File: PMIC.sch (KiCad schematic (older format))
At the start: 71 parts, among them U4 CSD86330Q3D, U5 LMR62014XMF_NOPB, U6 CSD86330Q3D, U8 TPS65086100

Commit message: Updated GPIO pinout to BV0.9. Remapped DSI. Mapped USB3.0
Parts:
- R121: footprint antmicro-footprints:0402-res -> arvsom-footprints:0402-res; symbol antmicroResistors0402:R_1k_0402 -> arvsom:R_1k_0402
- R123: footprint antmicro-footprints:0402-res -> arvsom-footprints:0402-res; symbol antmicroResistors0402:R_0R_0402 -> arvsom:R_0R_0402
- R13: footprint antmicro-footprints:0402-res -> arvsom-footprints:0402-res; symbol antmicroResistors0402:R_12k1_0402 -> arvsom:R_12k1_0402
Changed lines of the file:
@@
 	11025 6075 11375 6075
 $Comp
-L antmicroResistors0402:R_1k_0402 R121
+L arvsom:R_1k_0402 R121
 U 1 1 60BEDFDF
 P 3650 3750
 F 0 "R121" V 3700 4050 60  0000 R CNN
 F 1 "R_1k_0402" H 3650 3600 60  0001 C CNN
-F 2 "antmicro-footprints:0402-res" H 3850 3950 60  0001 L CNN
+F 2 "arvsom-footprints:0402-res" H 3850 3950 60  0001 L CNN
 F 3 "" H 3650 3750 50  0001 C CNN
 F 4 "BOURNS" H 3850 4150 60  0001 L CNN "Manufacturer"
@@
 Connection ~ 3925 4600
 $Comp
-L antmicroResistors0402:R_0R_0402 R123
+L arvsom:R_0R_0402 R123
 U 1 1 60C2519F
 P 5425 5575
 F 0 "R123" H 5375 5700 60  0000 C CNN
 F 1 "R_0R_0402" H 5425 5425 60  0001 C CNN
-F 2 "antmicro-footprints:0402-res" H 5625 5775 60  0001 L CNN
+F 2 "arvsom-footprints:0402-res" H 5625 5775 60  0001 L CNN
 F 3 "" H 5425 5575 50  0001 C CNN
 F 4 "PANASONIC" H 5625 5975 60  0001 L CNN "Manufacturer"
@@
 	5575 5575 5900 5575
 $Comp
-L antmicroResistors0402:R_12k1_0402 R13
+L arvsom:R_12k1_0402 R13
 U 1 1 60C62589
 P 8500 4475
 F 0 "R13" H 8275 4525 60  0000 C CNN
 F 1 "R_12k1_0402" H 8500 4325 60  0001 C CNN
-F 2 "antmicro-footprints:0402-res" H 8700 4675 60  0001 L CNN
+F 2 "arvsom-footprints:0402-res" H 8700 4675 60  0001 L CNN
 F 3 "" H 8500 4475 50  0001 C CNN
 F 4 "MULTICOMP" H 8700 4875 60  0001 L CNN "Manufacturer"

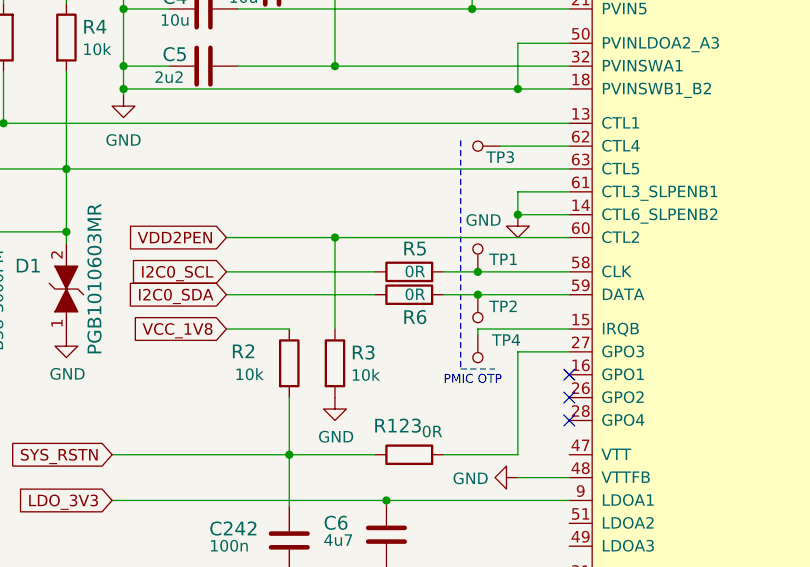
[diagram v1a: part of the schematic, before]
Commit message: Updated ethernet and interfaces.sch
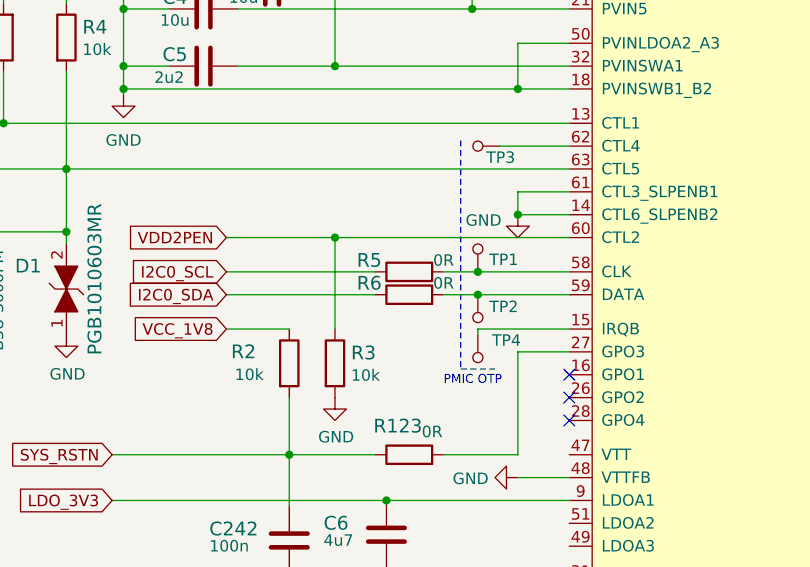
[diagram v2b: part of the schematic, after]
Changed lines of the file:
@@
 U 1 1 6073C6AC
 P 5425 4775
-F 0 "R5" H 5450 4875 60  0000 C CNN
+F 0 "R5" H 5250 4825 60  0000 C CNN
 F 1 "R_0R_0402" H 5425 4625 60  0001 C CNN
 F 2 "arvsom-footprints:0402-res" H 5625 4975 60  0001 L CNN
@@
 F 4 "PANASONIC" H 5625 5175 60  0001 L CNN "Manufacturer"
 F 5 "ERJ2GE0R00X" H 5625 5075 60  0001 L CNN "MPN"
-F 6 "0R" H 5450 4775 50  0000 C CNN "Val"
+F 6 "0R" H 5575 4825 50  0000 C CNN "Val"
 	1    5425 4775
 	1    0    0    -1
@@
 U 1 1 60743B7D
 P 5425 4875
-F 0 "R6" H 5450 4775 60  0000 C CNN
+F 0 "R6" H 5250 4925 60  0000 C CNN
 F 1 "R_0R_0402" H 5425 4725 60  0001 C CNN
 F 2 "arvsom-footprints:0402-res" H 5625 5075 60  0001 L CNN
@@
 F 4 "PANASONIC" H 5625 5275 60  0001 L CNN "Manufacturer"
 F 5 "ERJ2GE0R00X" H 5625 5175 60  0001 L CNN "MPN"
-F 6 "0R" H 5450 4875 50  0000 C CNN "Val"
+F 6 "0R" H 5575 4925 50  0000 C CNN "Val"
 	1    5425 4875
 	1    0    0    -1

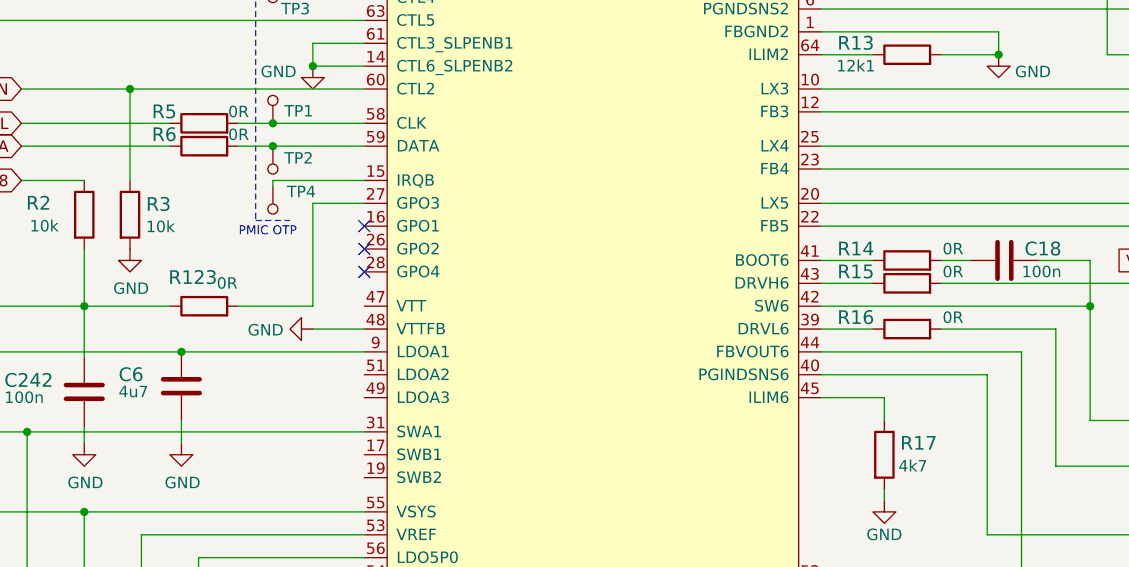
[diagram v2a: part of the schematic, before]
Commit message: Updated component placement - PHY passives placed, moved HDMI IC, lowered VIC and DDRs
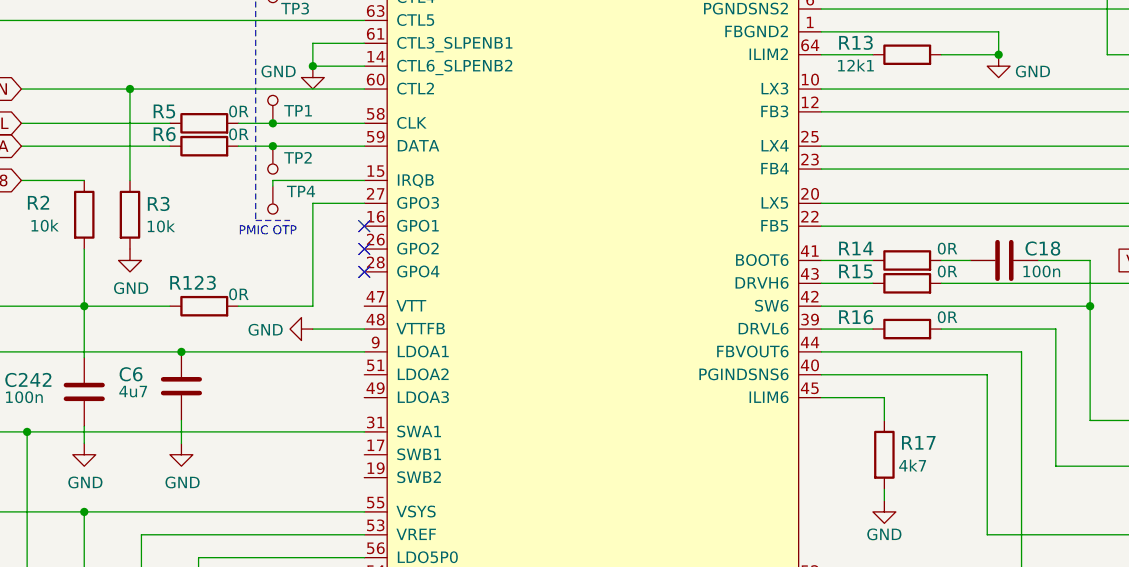
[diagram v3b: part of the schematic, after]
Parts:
- removed R10, R11, R12, R123, R14, R15, R16, R5, R6: R_0R_0402, arvsom-footprints:0402-res, symbol arvsom:R_0R_0402
- added R10, R11, R12, R123, R14, R15, R16, R5, R6: R_0R_0201, antmicro-footprints:0201-res, symbol antmicroResistorsmisc:R_0R_0201
- U8: footprint arvsom-footprints:QFN50P900X900X80-65N -> arvsom-footprints:S-PVQFN-N64
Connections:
- net I2C0_SCL: now also R5.1
- net I2C0_SDA: now also R6.1
- net SYS_RSTN: now also R123.1
- net at U8.27 (GPO3): now also R123.2
- net at U8.3 (DRVH2): now also R11.1
- net at U8.39 (DRVL6): now also R16.1
- net at U8.41 (BOOT6): now also R14.1
- net at U8.43 (DRVH6): now also R15.1
- net at U8.5 (BOOT2): now also R10.1
- net at TP1.1, U8.58 (CLK): now also R5.2
- net at TP2.1, U8.59 (DATA): now also R6.2
- net at U8.7 (DRVL2): now also R12.1
- net at C18.1: now also R14.2
- net at U6.3 (TG): now also R15.2
- net at U6.5 (BG): now also R16.2
- net at C17.1: now also R10.2
- net at U4.3 (TG): now also R11.2
- net at U4.5 (BG): now also R12.2
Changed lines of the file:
@@
 Text GLabel 4625 4875 0    50   Input ~ 0
 I2C0_SDA
-$Comp
-L arvsom:R_0R_0402 R5
-U 1 1 6073C6AC
-P 5425 4775
-F 0 "R5" H 5250 4825 60  0000 C CNN
-F 1 "R_0R_0402" H 5425 4625 60  0001 C CNN
-F 2 "arvsom-footprints:0402-res" H 5625 4975 60  0001 L CNN
-F 3 "" H 5425 4775 50  0001 C CNN
-F 4 "PANASONIC" H 5625 5175 60  0001 L CNN "Manufacturer"
-F 5 "ERJ2GE0R00X" H 5625 5075 60  0001 L CNN "MPN"
-F 6 "0R" H 5575 4825 50  0000 C CNN "Val"
-	1    5425 4775
-	1    0    0    -1
-$EndComp
-Wire Wire Line
-	4625 4775 5275 4775
 Wire Wire Line
 	5575 4775 5725 4775
-$Comp
-L arvsom:R_0R_0402 R6
-U 1 1 60743B7D
-P 5425 4875
-F 0 "R6" H 5250 4925 60  0000 C CNN
-F 1 "R_0R_0402" H 5425 4725 60  0001 C CNN
-F 2 "arvsom-footprints:0402-res" H 5625 5075 60  0001 L CNN
-F 3 "" H 5425 4875 50  0001 C CNN
-F 4 "PANASONIC" H 5625 5275 60  0001 L CNN "Manufacturer"
-F 5 "ERJ2GE0R00X" H 5625 5175 60  0001 L CNN "MPN"
-F 6 "0R" H 5575 4925 50  0000 C CNN "Val"
-	1    5425 4875
-	1    0    0    -1
-$EndComp
 Wire Wire Line
 	4625 4875 5275 4875
@@
 F 0 "U8" H 7125 3090 50  0000 C CNN
 F 1 "TPS65086100" H 7125 2999 50  0000 C CNN
-F 2 "arvsom-footprints:QFN50P900X900X80-65N" H 8025 2975 50  0001 C CNN
+F 2 "arvsom-footprints:S-PVQFN-N64" H 8025 2975 50  0001 C CNN
 F 3 "" H 6225 2925 50  0001 C CNN
 	1    6225 2925
@@
 $EndComp
 NoConn ~ 8125 3125
-$Comp
-L arvsom:R_0R_0402 R10
-U 1 1 608B362F
-P 8500 3775
-F 0 "R10" H 8275 3825 60  0000 C CNN
-F 1 "R_0R_0402" H 8500 3625 60  0001 C CNN
-F 2 "arvsom-footprints:0402-res" H 8700 3975 60  0001 L CNN
-F 3 "" H 8500 3775 50  0001 C CNN
-F 4 "PANASONIC" H 8700 4175 60  0001 L CNN "Manufacturer"
-F 5 "ERJ2GE0R00X" H 8700 4075 60  0001 L CNN "MPN"
-F 6 "0R" H 8675 3825 50  0000 C CNN "Val"
-	1    8500 3775
-	1    0    0    -1
-$EndComp
-$Comp
-L arvsom:R_0R_0402 R11
-U 1 1 608B4FA6
-P 8500 3875
-F 0 "R11" H 8275 3925 60  0000 C CNN
-F 1 "R_0R_0402" H 8500 3725 60  0001 C CNN
-F 2 "arvsom-footprints:0402-res" H 8700 4075 60  0001 L CNN
-F 3 "" H 8500 3875 50  0001 C CNN
-F 4 "PANASONIC" H 8700 4275 60  0001 L CNN "Manufacturer"
-F 5 "ERJ2GE0R00X" H 8700 4175 60  0001 L CNN "MPN"
-F 6 "0R" H 8675 3925 50  0000 C CNN "Val"
-	1    8500 3875
-	1    0    0    -1
-$EndComp
-$Comp
-L arvsom:R_0R_0402 R12
-U 1 1 608B665B
-P 8500 4075
-F 0 "R12" H 8275 4125 60  0000 C CNN
-F 1 "R_0R_0402" H 8500 3925 60  0001 C CNN
-F 2 "arvsom-footprints:0402-res" H 8700 4275 60  0001 L CNN
-F 3 "" H 8500 4075 50  0001 C CNN
-F 4 "PANASONIC" H 8700 4475 60  0001 L CNN "Manufacturer"
-F 5 "ERJ2GE0R00X" H 8700 4375 60  0001 L CNN "MPN"
-F 6 "0R" H 8675 4125 50  0000 C CNN "Val"
-	1    8500 4075
-	1    0    0    -1
-$EndComp
 Wire Wire Line
 	8125 3775 8350 3775
@@
 Wire Wire Line
 	8125 4625 10475 4625
-$Comp
-L arvsom:R_0R_0402 R14
-U 1 1 6080F73F
-P 8500 5375
-F 0 "R14" H 8275 5425 60  0000 C CNN
-F 1 "R_0R_0402" H 8500 5225 60  0001 C CNN
-F 2 "arvsom-footprints:0402-res" H 8700 5575 60  0001 L CNN
-F 3 "" H 8500 5375 50  0001 C CNN
-F 4 "PANASONIC" H 8700 5775 60  0001 L CNN "Manufacturer"
-F 5 "ERJ2GE0R00X" H 8700 5675 60  0001 L CNN "MPN"
-F 6 "0R" H 8700 5425 50  0000 C CNN "Val"
-	1    8500 5375
-	1    0    0    -1
-$EndComp
 Wire Wire Line
 	8125 5375 8350 5375
-$Comp
-L arvsom:R_0R_0402 R15
-U 1 1 60814E37
-P 8500 5475
-F 0 "R15" H 8275 5525 60  0000 C CNN
-F 1 "R_0R_0402" H 8500 5325 60  0001 C CNN
-F 2 "arvsom-footprints:0402-res" H 8700 5675 60  0001 L CNN
-F 3 "" H 8500 5475 50  0001 C CNN
-F 4 "PANASONIC" H 8700 5875 60  0001 L CNN "Manufacturer"
-F 5 "ERJ2GE0R00X" H 8700 5775 60  0001 L CNN "MPN"
-F 6 "0R" H 8700 5525 50  0000 C CNN "Val"
-	1    8500 5475
-	1    0    0    -1
-$EndComp
 Wire Wire Line
 	8125 5475 8350 5475
-$Comp
-L arvsom:R_0R_0402 R16
-U 1 1 6081A6B9
-P 8500 5675
-F 0 "R16" H 8275 5725 60  0000 C CNN
-F 1 "R_0R_0402" H 8500 5525 60  0001 C CNN
-F 2 "arvsom-footprints:0402-res" H 8700 5875 60  0001 L CNN
-F 3 "" H 8500 5675 50  0001 C CNN
-F 4 "PANASONIC" H 8700 6075 60  0001 L CNN "Manufacturer"
-F 5 "ERJ2GE0R00X" H 8700 5975 60  0001 L CNN "MPN"
-F 6 "0R" H 8700 5725 50  0000 C CNN "Val"
-	1    8500 5675
-	1    0    0    -1
-$EndComp
 Wire Wire Line
 	8125 5675 8350 5675
@@
 	3925 4600 3925 4325
 Connection ~ 3925 4600
-$Comp
-L arvsom:R_0R_0402 R123
-U 1 1 60C2519F
-P 5425 5575
-F 0 "R123" H 5375 5700 60  0000 C CNN
-F 1 "R_0R_0402" H 5425 5425 60  0001 C CNN
-F 2 "arvsom-footprints:0402-res" H 5625 5775 60  0001 L CNN
-F 3 "" H 5425 5575 50  0001 C CNN
-F 4 "PANASONIC" H 5625 5975 60  0001 L CNN "Manufacturer"
-F 5 "ERJ2GE0R00X" H 5625 5875 60  0001 L CNN "MPN"
-F 6 "0R" H 5525 5675 50  0000 C CNN "Val"
-	1    5425 5575
-	1    0    0    -1
-$EndComp
 Connection ~ 5325 5775
 Wire Wire Line
@@
 	1    0    0    -1
 $EndComp
+Wire Wire Line
+	4625 4775 5275 4775
+$Comp
+L antmicroResistorsmisc:R_0R_0201 R5
+U 1 1 60A1EF73
+P 5425 4775
+F 0 "R5" H 5250 4825 60  0000 C CNN
+F 1 "R_0R_0201" H 5425 4625 60  0001 C CNN
+F 2 "antmicro-footprints:0201-res" H 5625 4975 60  0001 L CNN
+F 3 "" H 5425 4775 50  0001 C CNN
+F 4 "VISHAY" H 5625 5175 60  0001 L CNN "Manufacturer"
+F 5 "CRCW02010000Z0ED" H 5625 5075 60  0001 L CNN "MPN"
+F 6 "0R" H 5575 4825 50  0000 C CNN "Val"
+	1    5425 4775
+	1    0    0    -1
+$EndComp
+$Comp
+L antmicroResistorsmisc:R_0R_0201 R6
+U 1 1 60A26BB5
+P 5425 4875
+F 0 "R6" H 5250 4925 60  0000 C CNN
+F 1 "R_0R_0201" H 5425 4725 60  0001 C CNN
+F 2 "antmicro-footprints:0201-res" H 5625 5075 60  0001 L CNN
+F 3 "" H 5425 4875 50  0001 C CNN
+F 4 "VISHAY" H 5625 5275 60  0001 L CNN "Manufacturer"
+F 5 "CRCW02010000Z0ED" H 5625 5175 60  0001 L CNN "MPN"
+F 6 "0R" H 5575 4925 50  0000 C CNN "Val"
+	1    5425 4875
+	1    0    0    -1
+$EndComp
+$Comp
+L antmicroResistorsmisc:R_0R_0201 R123
+U 1 1 60A2A03C
+P 5425 5575
+F 0 "R123" H 5375 5675 60  0000 C CNN
+F 1 "R_0R_0201" H 5425 5425 60  0001 C CNN
+F 2 "antmicro-footprints:0201-res" H 5625 5775 60  0001 L CNN
+F 3 "" H 5425 5575 50  0001 C CNN
+F 4 "VISHAY" H 5625 5975 60  0001 L CNN "Manufacturer"
+F 5 "CRCW02010000Z0ED" H 5625 5875 60  0001 L CNN "MPN"
+F 6 "0R" H 5575 5625 50  0000 C CNN "Val"
+	1    5425 5575
+	1    0    0    -1
+$EndComp
+$Comp
+L antmicroResistorsmisc:R_0R_0201 R10
+U 1 1 60A468A9
+P 8500 3775
+F 0 "R10" H 8275 3825 60  0000 C CNN
+F 1 "R_0R_0201" H 8500 3625 60  0001 C CNN
+F 2 "antmicro-footprints:0201-res" H 8700 3975 60  0001 L CNN
+F 3 "" H 8500 3775 50  0001 C CNN
+F 4 "VISHAY" H 8700 4175 60  0001 L CNN "Manufacturer"
+F 5 "CRCW02010000Z0ED" H 8700 4075 60  0001 L CNN "MPN"
+F 6 "0R" H 8675 3825 50  0000 C CNN "Val"
+	1    8500 3775
+	1    0    0    -1
+$EndComp
+$Comp
+L antmicroResistorsmisc:R_0R_0201 R11
+U 1 1 60A4B370
+P 8500 3875
+F 0 "R11" H 8275 3925 60  0000 C CNN
+F 1 "R_0R_0201" H 8500 3725 60  0001 C CNN
+F 2 "antmicro-footprints:0201-res" H 8700 4075 60  0001 L CNN
+F 3 "" H 8500 3875 50  0001 C CNN
+F 4 "VISHAY" H 8700 4275 60  0001 L CNN "Manufacturer"
+F 5 "CRCW02010000Z0ED" H 8700 4175 60  0001 L CNN "MPN"
+F 6 "0R" H 8675 3925 50  0000 C CNN "Val"
+	1    8500 3875
+	1    0    0    -1
+$EndComp
+$Comp
+L antmicroResistorsmisc:R_0R_0201 R12
+U 1 1 60A4C09F
+P 8500 4075
+F 0 "R12" H 8275 4125 60  0000 C CNN
+F 1 "R_0R_0201" H 8500 3925 60  0001 C CNN
+F 2 "antmicro-footprints:0201-res" H 8700 4275 60  0001 L CNN
+F 3 "" H 8500 4075 50  0001 C CNN
+F 4 "VISHAY" H 8700 4475 60  0001 L CNN "Manufacturer"
+F 5 "CRCW02010000Z0ED" H 8700 4375 60  0001 L CNN "MPN"
+F 6 "0R" H 8675 4125 50  0000 C CNN "Val"
+	1    8500 4075
+	1    0    0    -1
+$EndComp
+$Comp
+L antmicroResistorsmisc:R_0R_0201 R14
+U 1 1 60A523FE
+P 8500 5375
+F 0 "R14" H 8275 5425 60  0000 C CNN
+F 1 "R_0R_0201" H 8500 5225 60  0001 C CNN
+F 2 "antmicro-footprints:0201-res" H 8700 5575 60  0001 L CNN
+F 3 "" H 8500 5375 50  0001 C CNN
+F 4 "VISHAY" H 8700 5775 60  0001 L CNN "Manufacturer"
+F 5 "CRCW02010000Z0ED" H 8700 5675 60  0001 L CNN "MPN"
+F 6 "0R" H 8675 5425 50  0000 C CNN "Val"
+	1    8500 5375
+	1    0    0    -1
+$EndComp
+$Comp
+L antmicroResistorsmisc:R_0R_0201 R15
+U 1 1 60A56682
+P 8500 5475
+F 0 "R15" H 8275 5525 60  0000 C CNN
+F 1 "R_0R_0201" H 8500 5325 60  0001 C CNN
+F 2 "antmicro-footprints:0201-res" H 8700 5675 60  0001 L CNN
+F 3 "" H 8500 5475 50  0001 C CNN
+F 4 "VISHAY" H 8700 5875 60  0001 L CNN "Manufacturer"
+F 5 "CRCW02010000Z0ED" H 8700 5775 60  0001 L CNN "MPN"
+F 6 "0R" H 8675 5525 50  0000 C CNN "Val"
+	1    8500 5475
+	1    0    0    -1
+$EndComp
+$Comp
+L antmicroResistorsmisc:R_0R_0201 R16
+U 1 1 60A57367
+P 8500 5675
+F 0 "R16" H 8275 5725 60  0000 C CNN
+F 1 "R_0R_0201" H 8500 5525 60  0001 C CNN
+F 2 "antmicro-footprints:0201-res" H 8700 5875 60  0001 L CNN
+F 3 "" H 8500 5675 50  0001 C CNN
+F 4 "VISHAY" H 8700 6075 60  0001 L CNN "Manufacturer"
+F 5 "CRCW02010000Z0ED" H 8700 5975 60  0001 L CNN "MPN"
+F 6 "0R" H 8675 5725 50  0000 C CNN "Val"
+	1    8500 5675
+	1    0    0    -1
+$EndComp

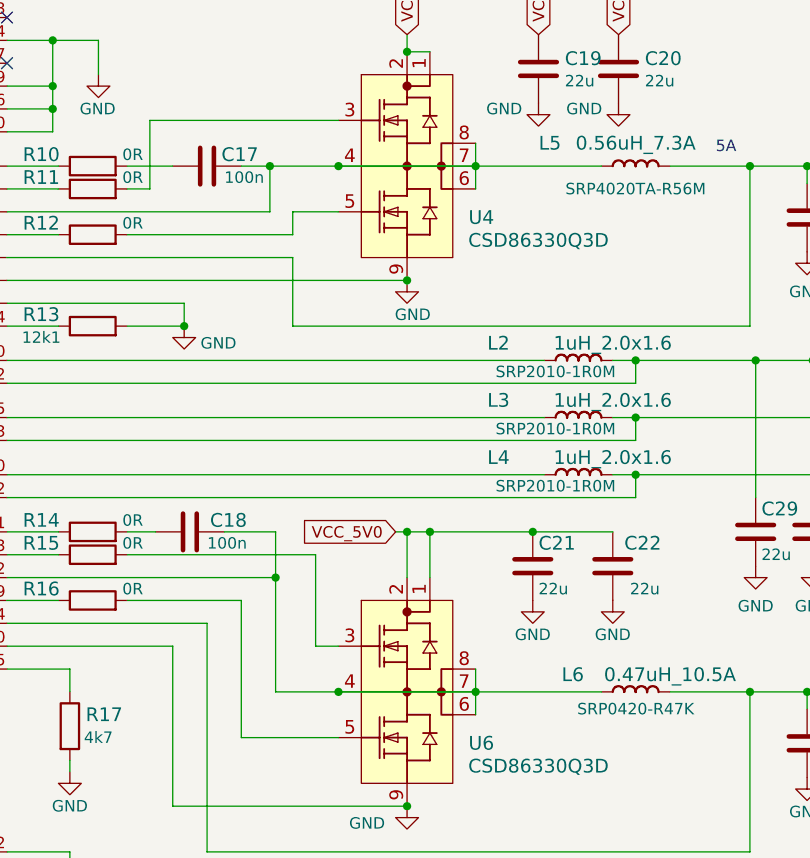
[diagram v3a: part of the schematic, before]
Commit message: PMIC re-worked, layout
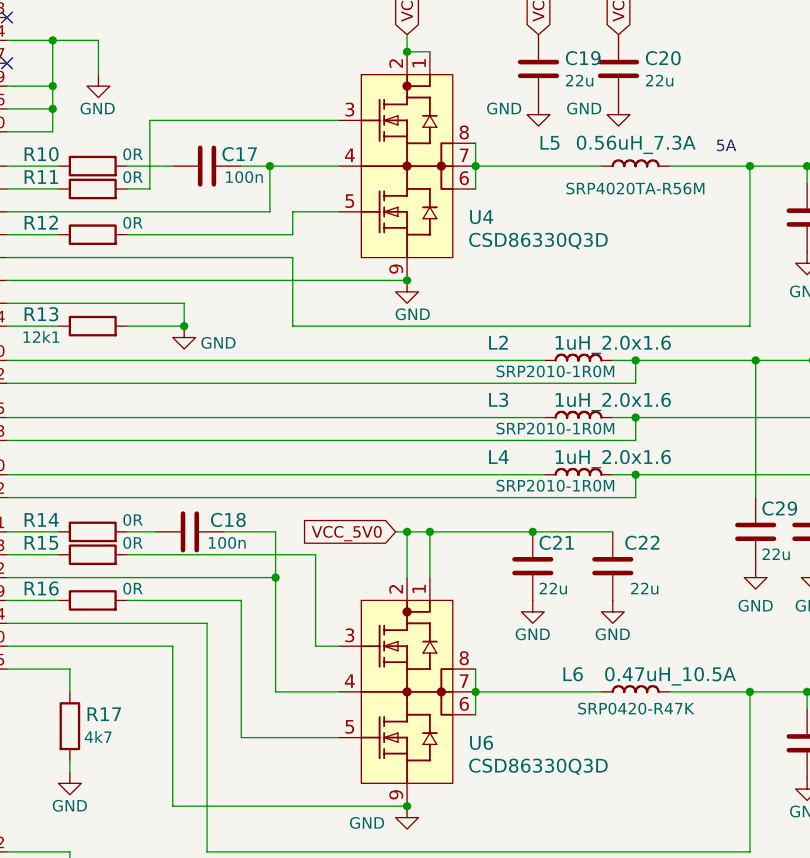
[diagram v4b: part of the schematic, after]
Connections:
- net at L5.1 (P), U4.6 (VSW), U4.7 (VSW)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: no longer C17.2, U4.4 (TGR), U8.4 (SW2)
- net at L6.1 (P), U6.6 (VSW), U6.7 (VSW)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: no longer C18.2, U6.4 (TGR), U8.42 (SW6)
- new net: C17.2, U4.4 (TGR), U8.4 (SW2)
- new net: C18.2, U6.4 (TGR), U8.42 (SW6)
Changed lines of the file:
@@
 	0    -1   -1   0
 $EndComp
-Wire Wire Line
-	9575 3775 10175 3775
 $Comp
 L arvsom:CSD86330Q3D U4
@@
 Wire Wire Line
 	9300 6075 9575 6075
-Connection ~ 9575 6075
-Wire Wire Line
-	9575 6075 10175 6075
 Connection ~ 10175 6075
 Wire Wire Line
@@
 Wire Wire Line
 	9575 3775 9275 3775
-Connection ~ 9575 3775
 Connection ~ 9275 3775
 Wire Wire Line
